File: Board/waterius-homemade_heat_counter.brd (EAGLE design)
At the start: 50.5 x 61.6 mm, 38 parts, among them IC1 TINY13-20SU, Q1 MMBTA92, Q2 MMBTA92, U1 RS-485-MODULE

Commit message: rewire1
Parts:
- moved JP4 42.7 mm to (11.4, 33.0), turned to 0 degrees
- moved R9 40.9 mm to (17.8, 31.1), turned to 0 degrees
- moved R11 35.6 mm to (17.8, 33.7), turned to 180 degrees
- moved JP5 35.6 mm to (49.5, 59.1), turned to 90 degrees
- moved R10 11.1 mm to (8.26, 58.4), turned to 0 degrees
- moved S1 7.62 mm to (11.4, 22.9), turned to 270 degrees
- moved JP1 6.48 mm to (49.5, 69.8), turned to 180 degrees
- moved LED1 4.84 mm to (43.8, 30.5), turned to 180 degrees
- moved Q2 3.18 mm to (40.0, 21.0)
- moved R15 2.84 mm to (41.9, 23.5), turned to 0 degrees
- moved R4 2.01 mm to (46.4, 30.5), turned to 90 degrees
- moved R16 1.80 mm to (45.7, 22.2), turned to 90 degrees
- moved R14 0.63 mm to (38.7, 59.7)
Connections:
- net +3V3: no longer Q2.2, R15.1
- net AA*3: now also Q2.2, R15.1
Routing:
- net GND: track 230.7 -> 292.8 mm, vias 5 -> 2
- net AA*3: track 18.0 -> 61.4 mm, vias 0 -> 2
- net WAKE_UP: track 56.3 -> 28.4 mm
- net N$5: track 16.7 -> 36.0 mm
- net N$1: track 11.8 -> 30.9 mm
- net EN_HC_VCC: track 48.4 -> 63.3 mm
- net N$7: track 28.2 -> 42.8 mm
- net GND1: track 58.1 -> 66.8 mm, vias 0 -> 2
- net VCC_RS485: track 4.23 -> 6.95 mm
- net +3V3: track 137.3 -> 139.8 mm
- net SCK: track 69.5 -> 71.8 mm
- net N$13: track 6.52 -> 8.51 mm
- net RS485_B: track 7.69 -> 6.61 mm
- net N$10: track 5.77 -> 5.14 mm

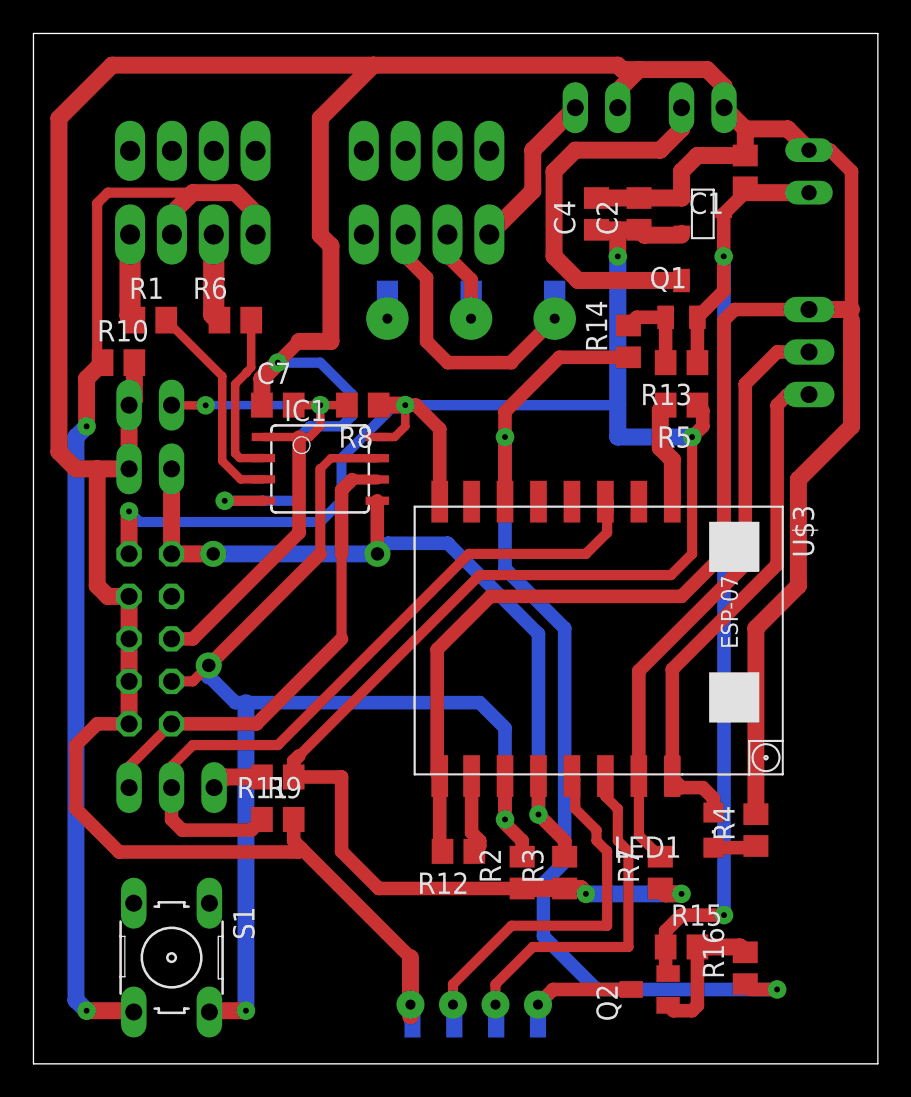
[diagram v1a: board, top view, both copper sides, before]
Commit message: remove 1 trans
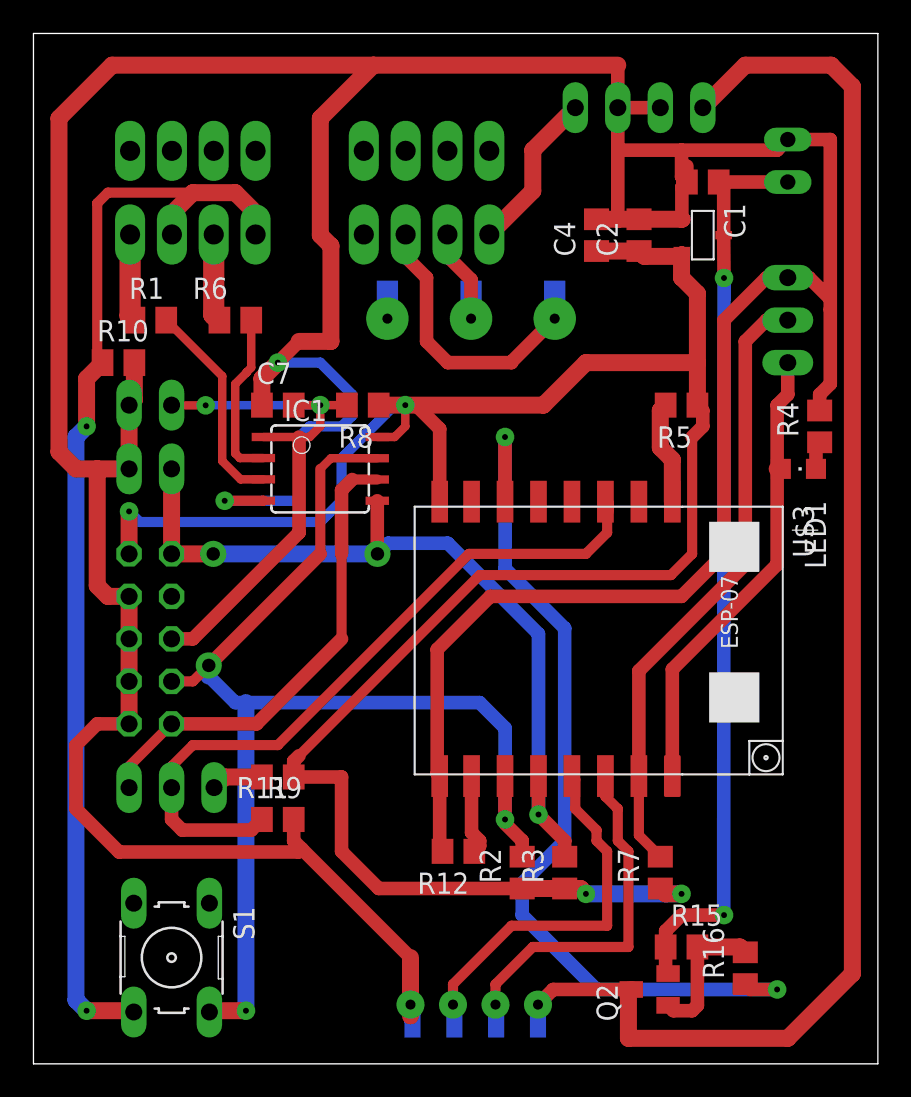
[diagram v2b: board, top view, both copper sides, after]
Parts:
- removed Q1: MMBTA92, semicon-smd-ipc:SOT23
- removed R13: 10k, rcl:R0805
- removed R14: 3k3, rcl:R0805
- moved R4 24.4 mm to (50.2, 54.6)
- moved LED1 22.2 mm to (48.9, 52.1), turned to 270 degrees
- moved C1 2.62 mm to (43.2, 69.2), turned to 180 degrees
- moved JP5 2.29 mm to (48.3, 61.0)
- moved JP1 1.42 mm to (48.3, 70.5)
- moved JP7 1.27 mm to (41.9, 73.7), turned to 0 degrees
- moved C2 1.27 mm to (39.4, 66.0)
- moved C4 1.27 mm to (36.8, 66.0)
- moved U$2 1.27 mm to (43.2, 66.0)
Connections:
- removed net N$10: Q1.1, R13.2, R14.2
- removed net VCC_DCDC_STEPUP: JP7.1, Q1.3
- net AA*3: no longer Q1.2, R13.1
- net EN_HC_VCC: no longer R14.1
- net VCC_RS485: now also JP7.1
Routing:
- net VCC_RS485: track 6.95 -> 88.5 mm
- net VCC_DCDC_STEPUP: track 23.2 -> 0.00 mm
- net GND: track 292.8 -> 272.1 mm
- net EN_HC_VCC: track 63.3 -> 54.1 mm
- net AA*3: track 61.4 -> 54.6 mm
- net N$10: track 5.14 -> 0.00 mm
- net N$1: track 30.9 -> 27.9 mm
- net +3V3: track 139.8 -> 138.1 mm, vias 6 -> 4
- net N$5: track 36.0 -> 37.0 mm
- net N$6: track 2.58 -> 1.68 mm
